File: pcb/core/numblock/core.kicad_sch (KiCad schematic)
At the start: 25 parts, among them J1 Conn_01x11, J2 Conn_01x11, SW1 SW_Push_45deg, SW2 SW_Push_45deg, SW3 SW_Push_45deg, SW4 SW_Push_45deg, SW5 SW_Push_45deg, SW6 SW_Push_45deg, SW7 SW_Push_45deg, SW8 SW_Push_45deg, SW9 SW_Push_45deg, U1 Helios

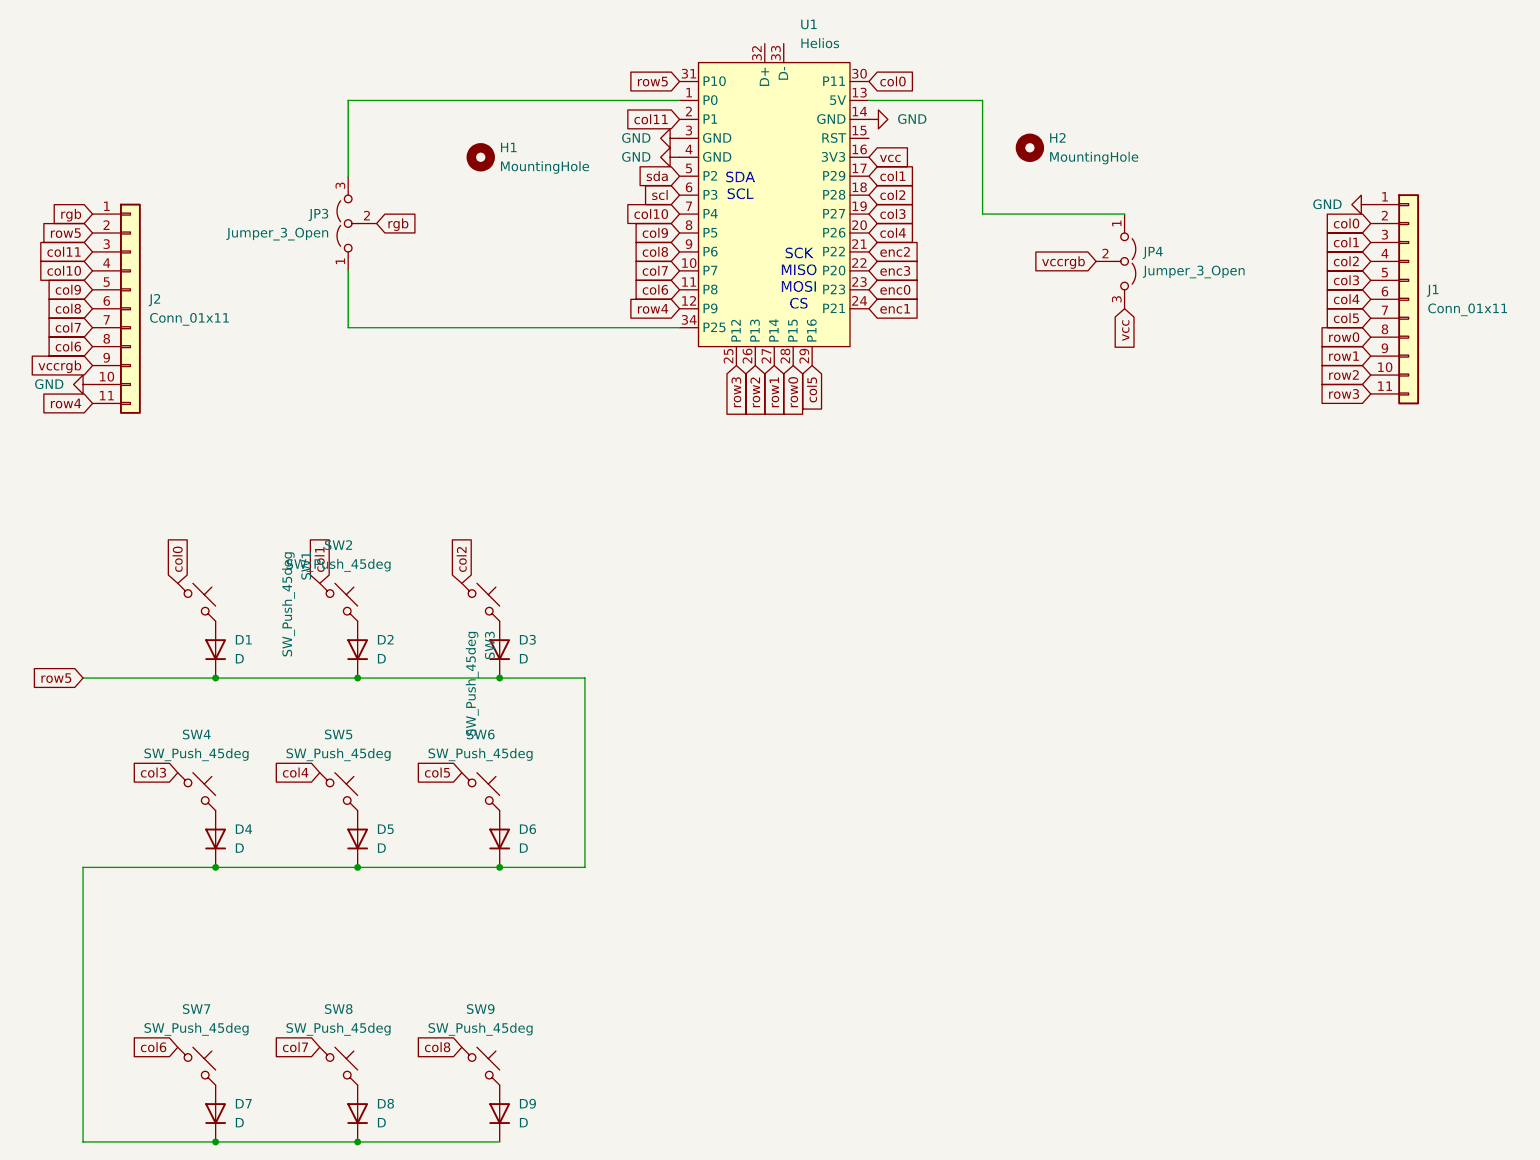
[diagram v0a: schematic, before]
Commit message: added break off key to the numpad core
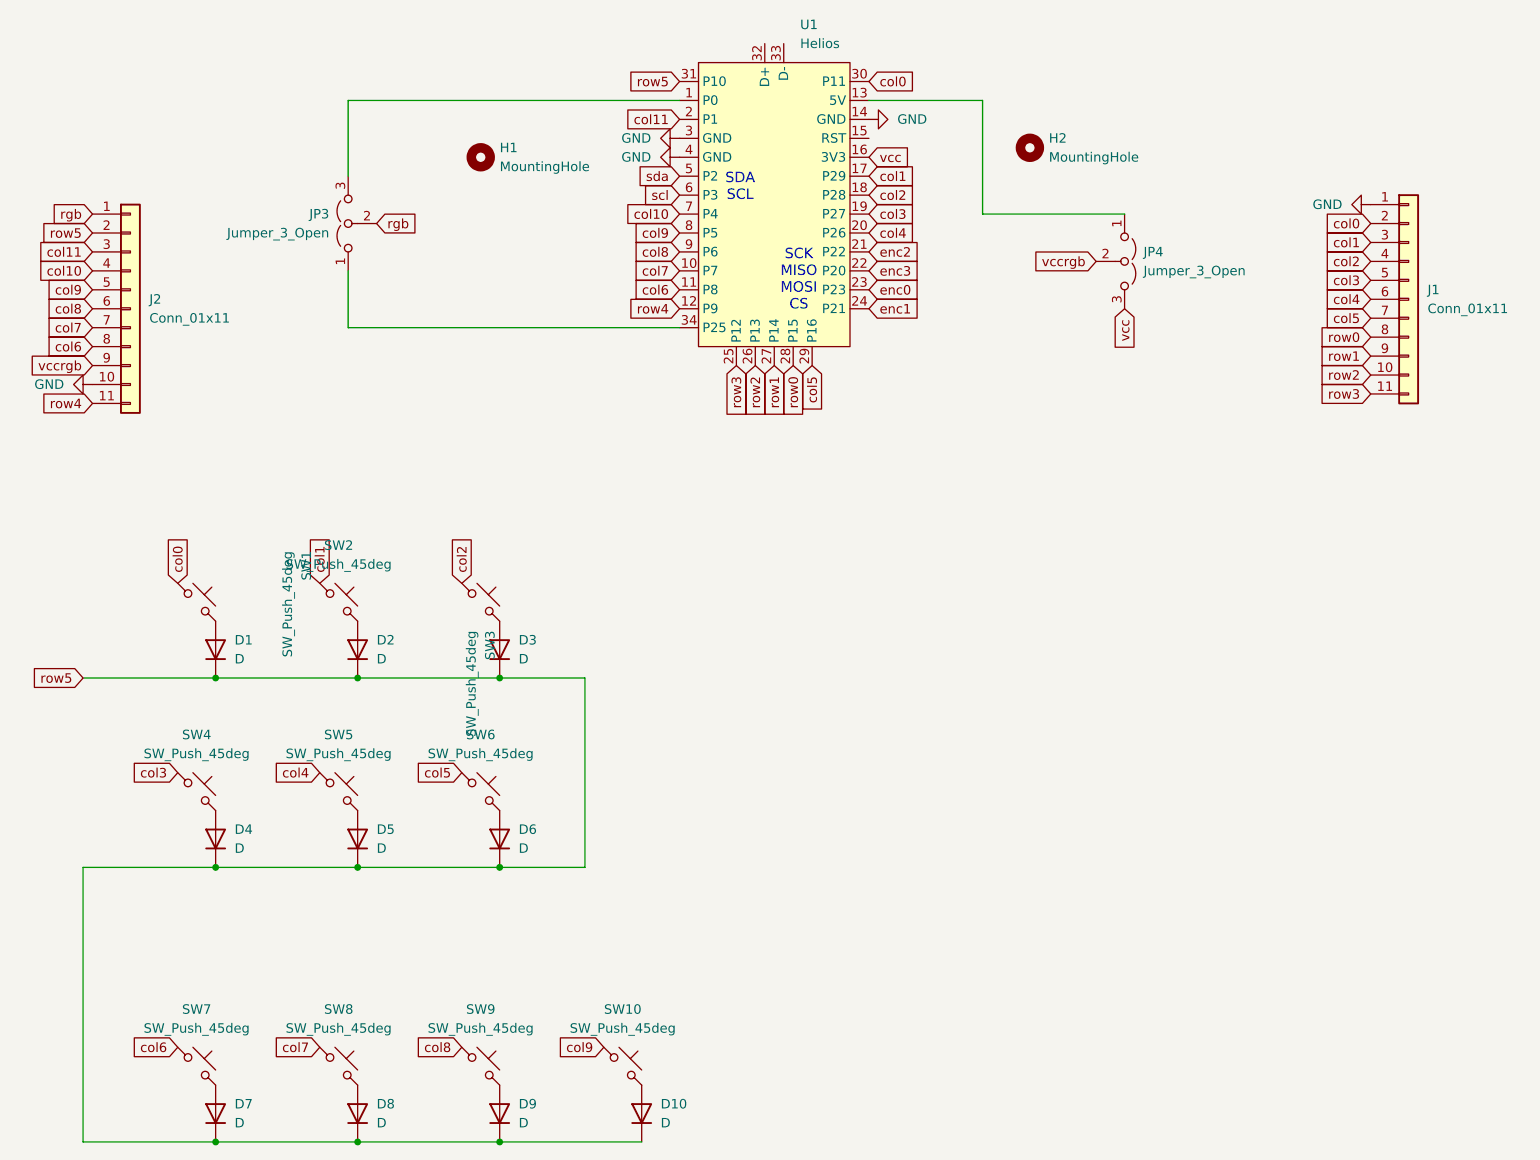
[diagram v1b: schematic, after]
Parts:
- added D10: D, barnacle:D_SOD-123-minimal, symbol Device:D
- added SW10: SW_Push_45deg, PCM_marbastlib-mx:SW_MX_HS_S_CPG151101S11_1u, symbol Switch:SW_Push_45deg
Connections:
- net col9: now also SW10.1
- net row5: now also D10.1 (K)
- new net: D10.2 (A), SW10.2
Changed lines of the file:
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@@
 (kicad_sch
-	(version 20231120)
+	(version 20250114)
 	(generator "eeschema")
-	(generator_version "8.0")
+	(generator_version "9.0")
 	(paper "A4")
+	(text "SDA\nSCL"
+		(exclude_from_sim no)
+		(at 132.588 51.054 0)
+		(effects
+			(font
+				(size 1.397 1.397)
+			)
+		)
+	)
+	(text "SCK\nMISO\nMOSI\nCS"
+		(exclude_from_sim no)
+		(at 140.462 63.5 0)
+		(effects
+			(font
+				(size 1.397 1.397)
+			)
+		)
+	)
 	(junction
 		(at 100.33 116.84)
@@
 	)
 	(junction
+		(at 100.33 179.07)
+		(diameter 0)
+		(color 0 0 0 0)
+	)
+	(junction
 		(at 62.23 179.07)
 		(diameter 0)
@@
 	(wire
 		(pts
+			(xy 100.33 179.07) (xy 119.38 179.07)
+		)
+		(stroke
+			(width 0)
+			(type default)
+		)
+	)
+	(wire
+		(pts
 			(xy 81.28 142.24) (xy 100.33 142.24)
 		)
@@
 		)
 	)
-	(text "SDA\nSCL"
-		(exclude_from_sim no)
-		(at 132.588 51.054 0)
-		(effects
-			(font
-				(size 1.397 1.397)
-			)
-		)
-	)
-	(text "SCK\nMISO\nMOSI\nCS"
-		(exclude_from_sim no)
-		(at 140.462 63.5 0)
-		(effects
-			(font
-				(size 1.397 1.397)
-			)
-		)
-	)
 	(global_label "col11"
 		(shape input)
@@
 		)
 	)
+	(global_label "col9"
+		(shape input)
+		(at 114.3 166.37 180)
+		(fields_autoplaced yes)
+		(effects
+			(font
+				(size 1.27 1.27)
+			)
+			(justify right)
+		)
+		(property "Intersheetrefs" "${INTERSHEET_REFS}"
+			(at 107.2025 166.37 0)
+			(effects
+				(font
+					(size 1.27 1.27)
+				)
+				(justify right)
+				(hide yes)
+			)
+		)
+	)
 	(global_label "col6"
 		(shape input)
@@
 	)
 	(symbol
+		(lib_id "Switch:SW_Push_45deg")
+		(at 116.84 168.91 0)
+		(unit 1)
+		(exclude_from_sim no)
+		(in_bom yes)
+		(on_board yes)
+		(dnp no)
+		(fields_autoplaced yes)
+		(property "Reference" "SW10"
+			(at 116.84 161.29 0)
+			(effects
+				(font
+					(size 1.27 1.27)
+				)
+			)
+		)
+		(property "Value" "SW_Push_45deg"
+			(at 116.84 163.83 0)
+			(effects
+				(font
+					(size 1.27 1.27)
+				)
+			)
+		)
+		(property "Footprint" "PCM_marbastlib-mx:SW_MX_HS_S_CPG151101S11_1u"
+			(at 116.84 168.91 0)
+			(effects
+				(font
+					(size 1.27 1.27)
+				)
+				(hide yes)
+			)
+		)
+		(property "Datasheet" "~"
+			(at 116.84 168.91 0)
+			(effects
+				(font
+					(size 1.27 1.27)
+				)
+				(hide yes)
+			)
+		)
+		(property "Description" "Push button switch, normally open, two pins, 45° tilted"
+			(at 116.84 168.91 0)
+			(effects
+				(font
+					(size 1.27 1.27)
+				)
+				(hide yes)
+			)
+		)
+		(pin "1"
+		)
+		(pin "2"
+		)
+		(instances
+			(project "core"
+				(path "/8ef1751a-3bdc-4956-a5e1-70d94fb666d4"
+					(reference "SW10")
+					(unit 1)
+				)
+			)
+		)
+	)
+	(symbol
 		(lib_id "Mechanical:MountingHole")
 		(at 97.79 46.99 0)
@@
 	)
 	(symbol
+		(lib_id "Device:D")
+		(at 119.38 175.26 90)
+		(unit 1)
+		(exclude_from_sim no)
+		(in_bom yes)
+		(on_board yes)
+		(dnp no)
+		(fields_autoplaced yes)
+		(property "Reference" "D10"
+			(at 121.92 173.9899 90)
+			(effects
+				(font
+					(size 1.27 1.27)
+				)
+				(justify right)
+			)
+		)
+		(property "Value" "D"
+			(at 121.92 176.5299 90)
+			(effects
+				(font
+					(size 1.27 1.27)
+				)
+				(justify right)
+			)
+		)
+		(property "Footprint" "barnacle:D_SOD-123-minimal"
+			(at 119.38 175.26 0)
+			(effects
+				(font
+					(size 1.27 1.27)
+				)
+				(hide yes)
+			)
+		)
+		(property "Datasheet" "~"
+			(at 119.38 175.26 0)
+			(effects
+				(font
+					(size 1.27 1.27)
+				)
+				(hide yes)
+			)
+		)
+		(property "Description" "Diode"
+			(at 119.38 175.26 0)
+			(effects
+				(font
+					(size 1.27 1.27)
+				)
+				(hide yes)
+			)
+		)
+		(property "Sim.Device" "D"
+			(at 119.38 175.26 0)
+			(effects
+				(font
+					(size 1.27 1.27)
+				)
+				(hide yes)
+			)
+		)
+		(property "Sim.Pins" "1=K 2=A"
+			(at 119.38 175.26 0)
+			(effects
+				(font
+					(size 1.27 1.27)
+				)
+				(hide yes)
+			)
+		)
+		(pin "1"
+		)
+		(pin "2"
+		)
+		(instances
+			(project "core"
+				(path "/8ef1751a-3bdc-4956-a5e1-70d94fb666d4"
+					(reference "D10")
+					(unit 1)
+				)
+			)
+		)
+	)
+	(symbol
 		(lib_id "power:GND")
 		(at 217.17 53.34 270)
@@
 		)
 	)
+	(embedded_fonts no)
 )
